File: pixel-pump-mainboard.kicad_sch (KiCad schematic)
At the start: 121 parts, among them J1 JST NC Valve, J10 BM10B-SRSS-TB(LF)(SN), J11 UART/SWD DNP, J12 TYPE-C-31-M-12, J2 JST NO Valve, J3 6P4C, J4 JST 3 Way Valve, J5 Jack-DC 12V, J6 Power Sw, J7 EXP1, J8 EXP2, J9 BM04B-SRSS-TBT(LF)(SN), Q1 BSS138, Q2 BSS138, Q3 BSS138, Q4 STN4NF20L, Q5 BSS138, SW1 BOOTSEL, U1 LD1117S33TR, U2 TPS62112RSAR, U3 W25Q128JVS, U4 RP2040, Y1 ABMM2-12.000MHZ-E2-T

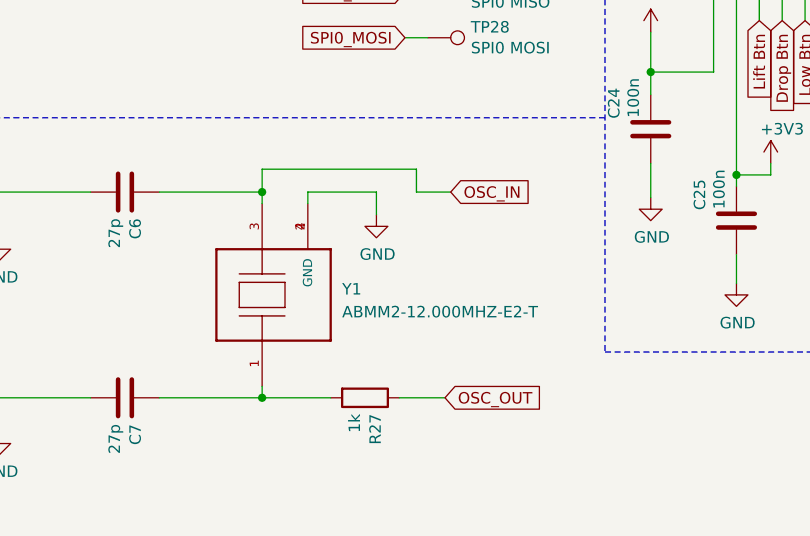
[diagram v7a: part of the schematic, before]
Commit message: Switch to CTS 445C25D12M00000 12 MHz crystal
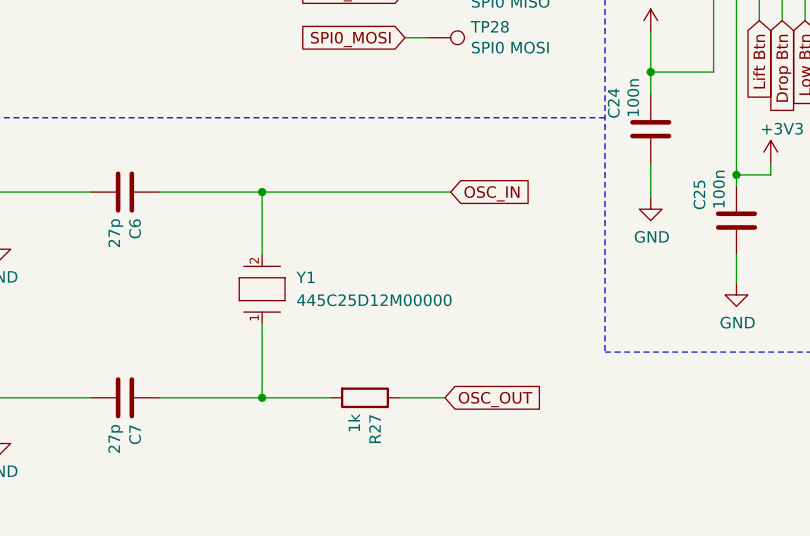
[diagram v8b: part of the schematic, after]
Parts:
- removed Y1: ABMM2-12.000MHZ-E2-T, ABMM2-12:XTAL_ABMM2-12.000MHZ-E2-T, symbol ABMM2-12.000MHZ-E2-T:ABMM2-12.000MHZ-E2-T
- added Y1: 445C25D12M00000, CTS 445C25D12M00000 12MHz:CTS-445-0-0-0, symbol CTS 445C25D12M00000 12MHz:445C25D12M00000
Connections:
- net OSC_IN: now also Y1.2
- net at C7.1, R27.2: now also Y1.1
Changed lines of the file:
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@@
   (junction (at 181.61 39.37) (diameter 0.9144) (color 0 0 0 0)
   )
+  (junction (at 231.14 248.285) (diameter 0) (color 0 0 0 0)
+  )
   (junction (at 362.585 40.005) (diameter 0.9144) (color 0 0 0 0)
   )
@@
   (junction (at 119.38 123.19) (diameter 0) (color 0 0 0 0)
   )
-  (junction (at 231.14 248.285) (diameter 0.9144) (color 0 0 0 0)
-  )
   (junction (at 294.005 37.465) (diameter 0.9144) (color 0 0 0 0)
   )
@@
     (stroke (width 0) (type solid) (color 0 0 0 0))
   )
-  (wire (pts (xy 231.14 248.285) (xy 231.14 249.555))
-    (stroke (width 0) (type solid) (color 0 0 0 0))
-  )
   (wire (pts (xy 197.485 182.245) (xy 197.485 177.165))
     (stroke (width 0) (type solid) (color 0 0 0 0))
   )
-  (wire (pts (xy 236.22 248.285) (xy 243.84 248.285))
-    (stroke (width 0) (type solid) (color 0 0 0 0))
-  )
-  (wire (pts (xy 243.84 248.285) (xy 243.84 250.825))
-    (stroke (width 0) (type solid) (color 0 0 0 0))
-  )
-  (wire (pts (xy 236.22 249.555) (xy 236.22 248.285))
-    (stroke (width 0) (type solid) (color 0 0 0 0))
-  )
   (wire (pts (xy 374.015 111.76) (xy 379.73 111.76))
     (stroke (width 0) (type solid) (color 0 0 0 0))
@@
     (stroke (width 0) (type solid) (color 0 0 0 0))
   )
-  (wire (pts (xy 252.095 248.285) (xy 248.285 248.285))
-    (stroke (width 0) (type solid) (color 0 0 0 0))
-  )
-  (wire (pts (xy 248.285 245.745) (xy 231.14 245.745))
-    (stroke (width 0) (type solid) (color 0 0 0 0))
-  )
-  (wire (pts (xy 248.285 248.285) (xy 248.285 245.745))
-    (stroke (width 0) (type solid) (color 0 0 0 0))
-  )
-  (wire (pts (xy 231.14 245.745) (xy 231.14 248.285))
-    (stroke (width 0) (type solid) (color 0 0 0 0))
-  )
   (wire (pts (xy 58.42 62.865) (xy 58.42 60.325))
     (stroke (width 0) (type solid) (color 0 0 0 0))
@@
     (stroke (width 0) (type dash) (color 0 0 0 0))
   )
+  (wire (pts (xy 231.14 248.285) (xy 252.095 248.285))
+    (stroke (width 0) (type default) (color 0 0 0 0))
+  )
   (wire (pts (xy 217.805 147.32) (xy 217.805 150.495))
     (stroke (width 0) (type solid) (color 0 0 0 0))
@@
     (stroke (width 0) (type solid) (color 0 0 0 0))
   )
+  (wire (pts (xy 231.14 248.285) (xy 231.14 255.27))
+    (stroke (width 0) (type default) (color 0 0 0 0))
+  )
   (wire (pts (xy 116.205 49.53) (xy 116.205 39.37))
     (stroke (width 0) (type solid) (color 0 0 0 0))
@@
     (stroke (width 0) (type solid) (color 0 0 0 0))
   )
-  (wire (pts (xy 231.14 271.145) (xy 231.14 269.875))
+  (wire (pts (xy 231.14 262.89) (xy 231.14 271.145))
     (stroke (width 0) (type solid) (color 0 0 0 0))
   )
@@
     (pin "2")
   )
-  (symbol (lib_id "power:GND") (at 243.84 250.825 0) (unit 1)
-    (in_bom yes) (on_board yes)
-    (property "Reference" "#PWR044" (id 0) (at 243.84 257.175 0)
-      (effects (font (size 1.27 1.27)) hide)
-    )
-    (property "Value" "GND" (id 1) (at 243.967 255.2192 0))
-    (property "Footprint" "" (id 2) (at 243.84 250.825 0)
-      (effects (font (size 1.27 1.27)) hide)
-    )
-    (property "Datasheet" "" (id 3) (at 243.84 250.825 0)
-      (effects (font (size 1.27 1.27)) hide)
-    )
-    (pin "1")
-  )
   (symbol (lib_id "Connector:TestPoint") (at 212.725 219.075 270) (unit 1)
     (in_bom yes) (on_board yes)
@@
     (pin "2")
   )
-  (symbol (lib_id "ABMM2-12.000MHZ-E2-T:ABMM2-12.000MHZ-E2-T") (at 231.14 259.715 90) (unit 1)
-    (in_bom yes) (on_board yes)
-    (property "Reference" "Y1" (id 0) (at 240.03 259.08 90)
-      (effects (font (size 1.27 1.27)) (justify right))
-    )
-    (property "Value" "ABMM2-12.000MHZ-E2-T" (id 1) (at 240.03 261.62 90)
-      (effects (font (size 1.27 1.27)) (justify right))
-    )
-    (property "Footprint" "ABMM2-12:XTAL_ABMM2-12.000MHZ-E2-T" (id 2) (at 231.14 259.715 0)
-      (effects (font (size 1.27 1.27)) (justify left bottom) hide)
-    )
-    (property "Datasheet" "" (id 3) (at 231.14 259.715 0)
-      (effects (font (size 1.27 1.27)) (justify left bottom) hide)
-    )
-    (property "MAXIMUM_PACKAGE_HEIGHT" "1.20 mm" (id 4) (at 231.14 259.715 0)
-      (effects (font (size 1.27 1.27)) (justify left bottom) hide)
-    )
-    (property "STANDARD" "Manufacturer Recommendations" (id 5) (at 231.14 259.715 0)
-      (effects (font (size 1.27 1.27)) (justify left bottom) hide)
-    )
-    (property "PARTREV" "01.18.13" (id 6) (at 231.14 259.715 0)
-      (effects (font (size 1.27 1.27)) (justify left bottom) hide)
-    )
-    (property "MANUFACTURER" "Abracon Corporation" (id 7) (at 231.14 259.715 0)
-      (effects (font (size 1.27 1.27)) (justify left bottom) hide)
-    )
-    (pin "1")
-    (pin "2")
-    (pin "3")
-    (pin "4")
-  )
   (symbol (lib_id "power:+12V") (at 252.095 57.15 0) (unit 1)
     (in_bom yes) (on_board yes)
@@
     (pin "1")
   )
+  (symbol (lib_id "CTS 445C25D12M00000 12MHz:445C25D12M00000") (at 231.14 262.89 90) (unit 1)
+    (in_bom yes) (on_board yes) (fields_autoplaced)
+    (property "Reference" "Y1" (id 0) (at 234.95 257.8099 90)
+      (effects (font (size 1.27 1.27)) (justify right))
+    )
+    (property "Value" "445C25D12M00000" (id 1) (at 234.95 260.3499 90)
+      (effects (font (size 1.27 1.27)) (justify right))
+    )
+    (property "Footprint" "CTS 445C25D12M00000 12MHz:CTS-445-0-0-0" (id 2) (at 220.98 262.89 0)
+      (effects (font (size 1.27 1.27)) (justify left) hide)
+    )
+    (property "Datasheet" "https://www.ctscorp.com/wp-content/uploads/445.pdf" (id 3) (at 218.44 262.89 0)
+      (effects (font (size 1.27 1.27)) (justify left) hide)
+    )
+    (property "category" "Crys" (id 4) (at 215.9 262.89 0)
+      (effects (font (size 1.27 1.27)) (justify left) hide)
+    )
+    (property "digikey description" "CRYSTAL 12.0000MHZ 18PF SMD" (id 5) (at 213.36 262.89 0)
+      (effects (font (size 1.27 1.27)) (justify left) hide)
+    )
+    (property "digikey part number" "CTX1162CT-ND" (id 6) (at 210.82 262.89 0)
+      (effects (font (size 1.27 1.27)) (justify left) hide)
+    )
+    (property "ipc land pattern name" "CAPC640320X60" (id 7) (at 208.28 262.89 0)
+      (effects (font (size 1.27 1.27)) (justify left) hide)
+    )
+    (property "lead free" "yes" (id 8) (at 205.74 262.89 0)
+      (effects (font (size 1.27 1.27)) (justify left) hide)
+    )
+    (property "library id" "a5a18dbfeb55b9dc" (id 9) (at 203.2 262.89 0)
+      (effects (font (size 1.27 1.27)) (justify left) hide)
+    )
+    (property "manufacturer" "CTS" (id 10) (at 200.66 262.89 0)
+      (effects (font (size 1.27 1.27)) (justify left) hide)
+    )
+    (property "mouser description" "Crystals 12MHz +/-20ppm 18pF -20C +70C" (id 11) (at 198.12 262.89 0)
+      (effects (font (size 1.27 1.27)) (justify left) hide)
+    )
+    (property "mouser part number" "774-445C25D12M00000" (id 12) (at 195.58 262.89 0)
+      (effects (font (size 1.27 1.27)) (justify left) hide)
+    )
+    (property "package" "SMD2" (id 13) (at 193.04 262.89 0)
+      (effects (font (size 1.27 1.27)) (justify left) hide)
+    )
+    (property "rohs" "yes" (id 14) (at 190.5 262.89 0)
+      (effects (font (size 1.27 1.27)) (justify left) hide)
+    )
+    (property "temperature range high" "+70°C" (id 15) (at 187.96 262.89 0)
+      (effects (font (size 1.27 1.27)) (justify left) hide)
+    )
+    (property "temperature range low" "-20°C" (id 16) (at 185.42 262.89 0)
+      (effects (font (size 1.27 1.27)) (justify left) hide)
+    )
+    (pin "1")
+    (pin "2")
+  )
   (symbol (lib_id "Device:C") (at 380.365 36.195 180) (unit 1)
     (in_bom yes) (on_board yes)
@@
       (reference "#PWR043") (unit 1) (value "GND") (footprint "")
     )
-    (path "/4abdfed4-255b-4d73-93a6-3950724f33f6"
-      (reference "#PWR044") (unit 1) (value "GND") (footprint "")
-    )
     (path "/0e223523-4391-45e7-9bb3-b2122631cec9"
       (reference "#PWR045") (unit 1) (value "GND") (footprint "")
@@
       (reference "U4") (unit 1) (value "RP2040") (footprint "RP2040:RP2040-QFN-56")
     )
-    (path "/6d397e23-9780-4ef8-bd21-217fd029665e"
-      (reference "Y1") (unit 1) (value "ABMM2-12.000MHZ-E2-T") (footprint "ABMM2-12:XTAL_ABMM2-12.000MHZ-E2-T")
+    (path "/db8d6a05-f70e-480e-9940-340484e3d966"
+      (reference "Y1") (unit 1) (value "445C25D12M00000") (footprint "CTS 445C25D12M00000 12MHz:CTS-445-0-0-0")
     )
   )
